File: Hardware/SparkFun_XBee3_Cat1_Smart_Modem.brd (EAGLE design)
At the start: 45.7 x 63.5 mm, 140 parts, among them J1 USB Female Type C Connector, J3 USB Female Type C Connector, J4 QWIIC_RIGHT_ANGLE, Q2 3.1A/30V/105mΩ, U1 FSUSB30MUX_MSOP10, U2 AP63203, U3 ESD Diode, U5 ESD Diode, U6 CP210X

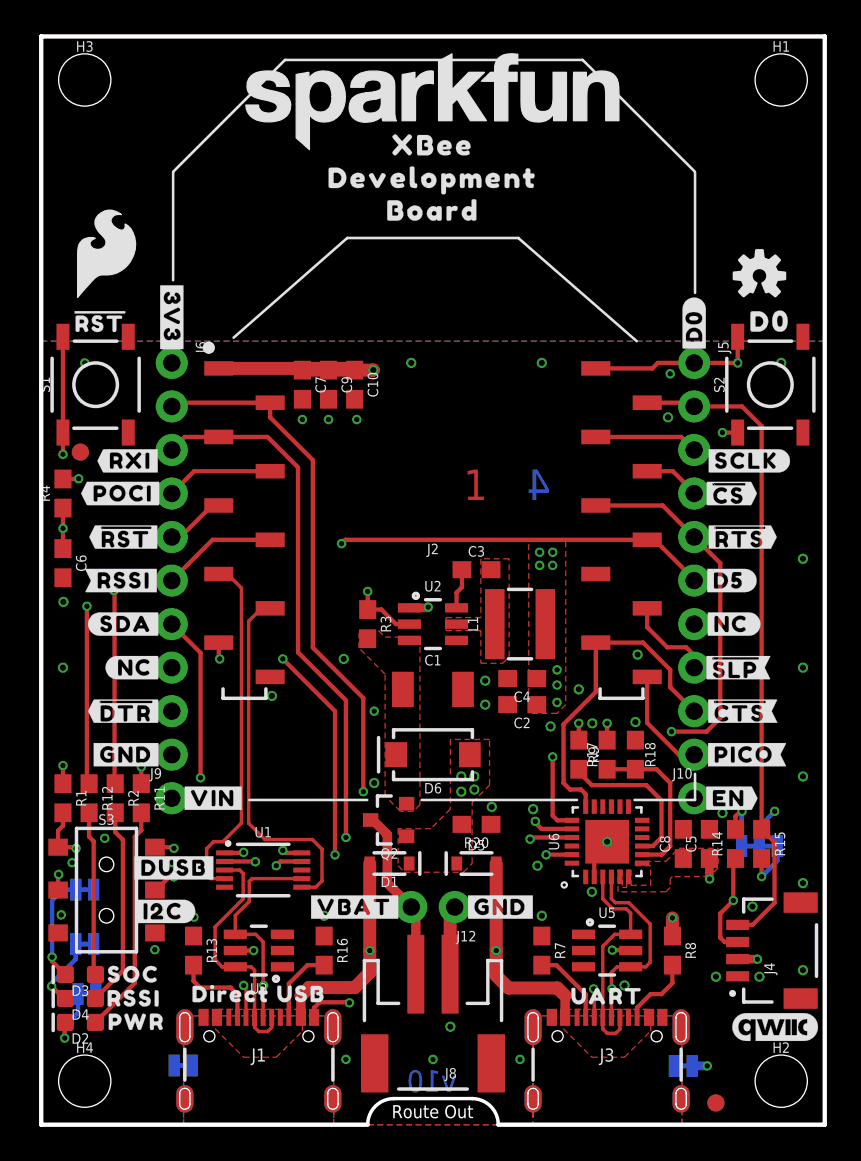
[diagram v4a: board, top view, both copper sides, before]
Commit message: Updates design to use the FT231XS instead of the CP2102N
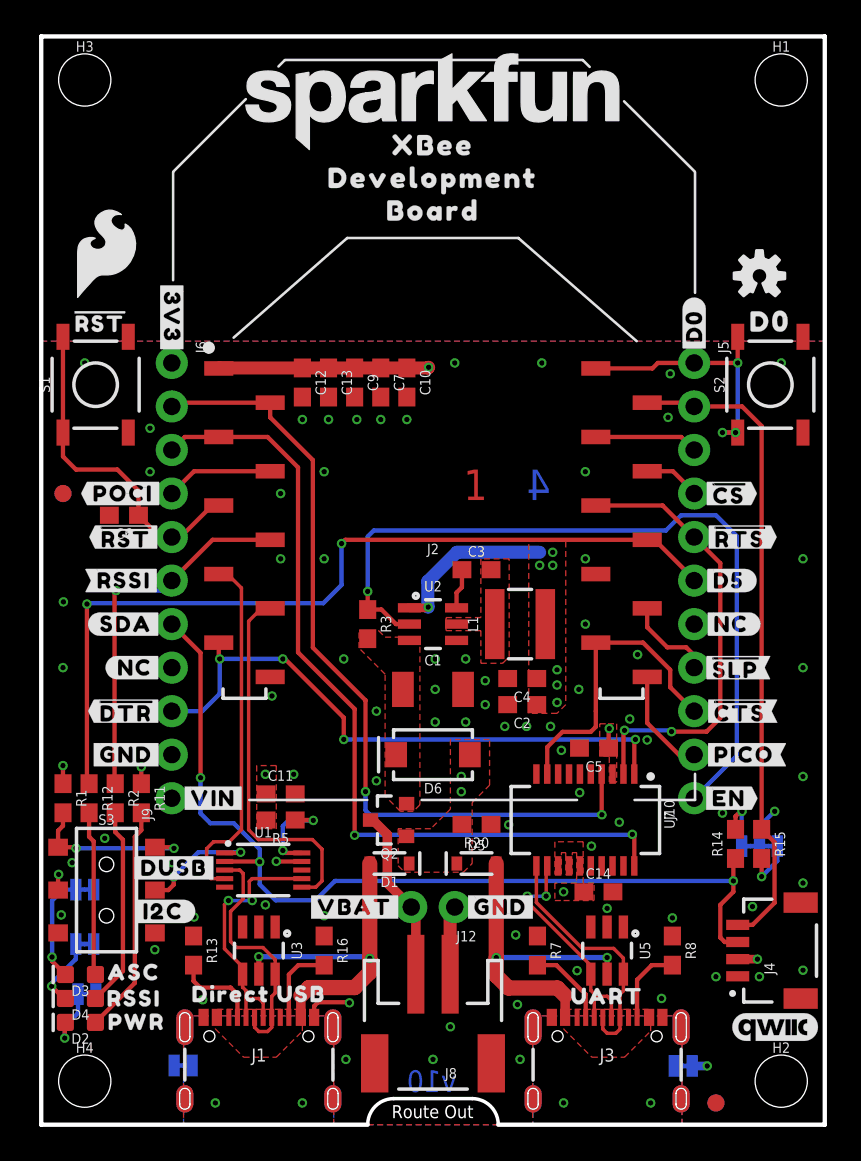
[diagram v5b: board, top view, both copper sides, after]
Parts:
- removed C8: 4.7uF, SparkFun-Capacitors:0603
- removed R17: 22k, SparkFun-Resistors:0603
- removed R18: 33k, SparkFun-Resistors:0603
- removed R4, R9: 10k, SparkFun-Resistors:0603
- removed U$19: (no value), top:#D2#AD2#19
- removed U$33: (no value), top:#SCLK#18
- removed U6: CP210X, SparkFun-IC-Comms:QFN24
- added C11, C14: 0.1uF, SparkFun-Capacitors:0603
- added C12: 10pF, SparkFun-Capacitors:0603
- added C13: 47pF, SparkFun-Capacitors:0603
- added R5: 100, SparkFun-Resistors:0603
- added U7: FT231XS, SparkFun-IC-Comms:SSOP20_L
- D4: value BLUE -> Yellow
- U$1: device top:#RXI#14 -> top:#D2#AD2#SCLK#19
- U$43: device topmirror:SOC30 -> top:ASC32
- moved U$1 26.6 mm to (31.8, 39.4), flipped to the bottom
- moved C5 8.75 mm to (32.3, 22.0), turned to 180 degrees
- moved C7 4.57 mm to (19.8, 43.3)
- moved C6 4.52 mm to (4.83, 35.6), turned to 180 degrees
- moved C10 3.05 mm to (21.3, 43.3)
- moved FD1 2.62 mm to (1.27, 36.8)
- moved FD2 2.62 mm to (1.27, 36.8)
- moved C9 1.53 mm to (18.3, 43.3)
- moved R7 0.25 mm to (29.0, 10.2)
- moved U$43 0.13 mm to (5.41, 8.89)
- turned J10 to 90 degrees
- turned J9 to 90 degrees
- turned U3 to 180 degrees
- turned U5 to 180 degrees
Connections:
- removed net N$10: R17.1, R18.2, U6.8
- removed net N$9: R9.2, U6.9
- new net N$3: R5.1, U1.10
- net !RESET!: no longer R4.1
- net 3.3V: now also C11.1, C12.1, C13.1, C14.1, R5.2; no longer C8.1, R4.2, R9.1, U1.10, U6.5, U6.6, U6.7
- net D+: now also U7.11; no longer U6.3
- net D-: now also U7.12; no longer U6.4
- net D13/TXO: now also U7.4; no longer U6.20
- net D14/RXI: now also U7.20; no longer U6.21
- net D6/!RTS!: now also U7.2; no longer U6.19
- net D7/!CTS!: now also U7.9; no longer U6.18
- net D8/!DTR!: now also U7.1; no longer U6.23
- net GND: now also C11.2, C12.2, C13.2, C14.2, U7.13, U7.14, U7.15, U7.16, U7.3, U7.6; no longer C8.2, R18.1, U6.2, U6.PAD
- net VIN: no longer R17.2
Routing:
- net VIN: track 28.2 -> 17.4 mm, vias 5 -> 2
- net N$10: track 9.54 -> 0.00 mm
- net N$9: track 9.17 -> 0.00 mm
- net D6/!RTS!: track 33.1 -> 26.2 mm
- net N$3: track 0.00 -> 5.57 mm, vias 0 -> 2
- net D14/RXI: track 44.4 -> 49.4 mm
- net D13/TXO: track 44.1 -> 48.2 mm
- net !RESET!: track 23.6 -> 20.1 mm, vias 2 -> 0
- net GND: track 12.7 -> 9.42 mm, vias 53 -> 77
- net 3.3V: track 31.8 -> 29.2 mm, vias 17 -> 15
- net D+: track 13.1 -> 14.7 mm
- net D7/!CTS!: track 19.2 -> 17.8 mm
- net D8/!DTR!: track 36.4 -> 35.2 mm
- net DIRECT_D-: track 15.9 -> 15.1 mm
- net D0: vias 2 -> 3
- added copper zone on layer 15, net SHLD
- added copper zone on layer 2, net SHLD
- added copper zone on layer 15, net SHLD1
- added copper zone on layer 2, net SHLD1

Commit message: Adds new 3.9uH Inductor
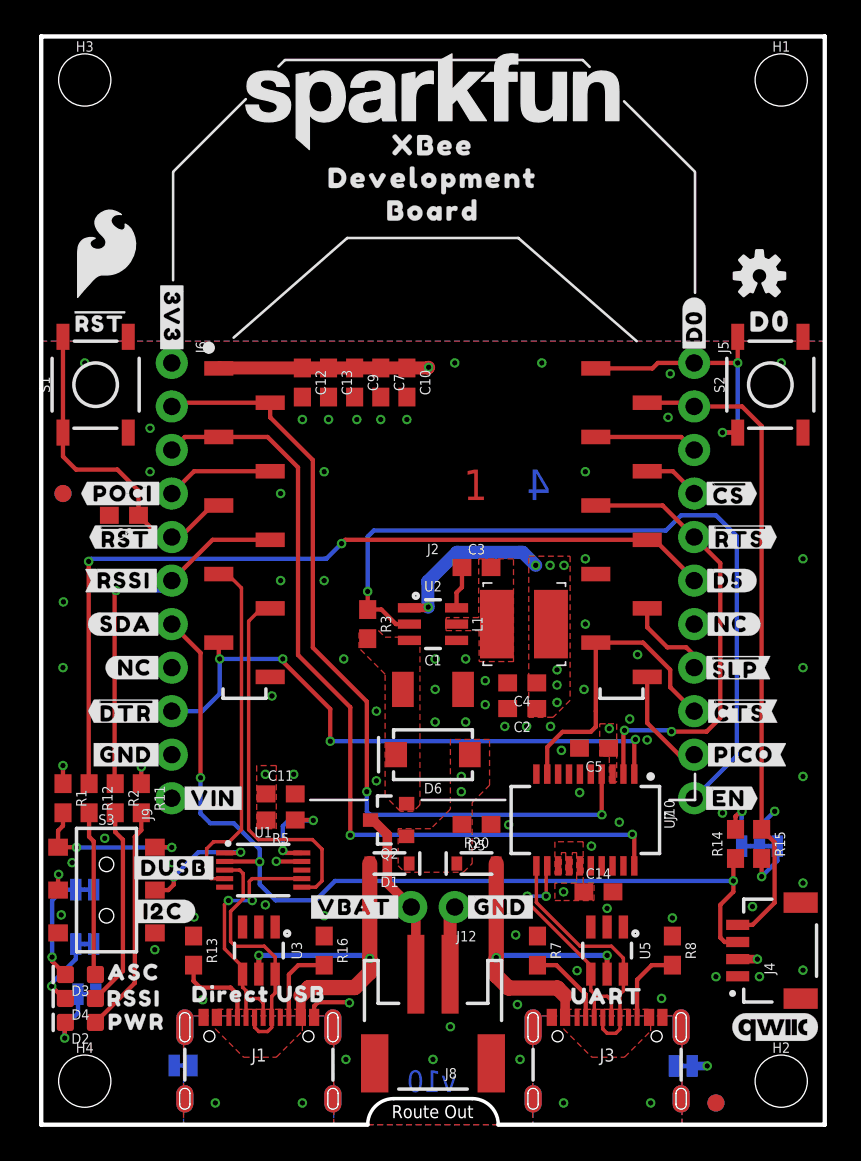
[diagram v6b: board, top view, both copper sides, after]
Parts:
- L1: value 4.7μH -> 3.9uH; device SparkFun-Coils:INDUCTOR_4X4MM -> SparkFun-Coils:INDUCTOR_3.9UH
- moved C4 0.25 mm to (28.1, 25.8)
- moved L1 0.25 mm to (28.2, 29.2)
- moved C2 0.23 mm to (28.1, 24.3)
- moved C3 0.13 mm to (25.4, 32.5)
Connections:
- net 3.3V: now also U7.13, U7.14, U7.15, U7.3
- net GND: no longer U7.13, U7.14, U7.15, U7.3
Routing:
- net 3.3V: track 29.2 -> 27.8 mm
- net D-: track 14.2 -> 13.7 mm
- net D8/!DTR!: track 35.2 -> 35.7 mm
- net D0: vias 3 -> 2

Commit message: Fixes swapped labels on LED jumpers
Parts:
- moved U$27 3.17 mm to (6.10, 13.7)
- moved U$64 3.17 mm to (5.97, 10.5)
- moved U$63 1.27 mm to (22.9, 59.7)
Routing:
- net GND: vias 77 -> 80
- removed copper zone on layer 15, net VIN
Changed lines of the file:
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@@
 <setting verticaltext="up"/>
 </settings>
-<grid distance="0.05" unitdist="inch" unit="inch" style="dots" multiple="1" display="yes" altdistance="0.001" altunitdist="inch" altunit="inch"/>
+<grid distance="0.05" unitdist="inch" unit="inch" style="dots" multiple="1" display="yes" altdistance="0.005" altunitdist="inch" altunit="inch"/>
 <layers>
 <layer number="1" name="Top" color="4" fill="1" visible="yes" active="yes"/>
@@
 <layer number="39" name="tKeepout" color="4" fill="11" visible="no" active="yes"/>
 <layer number="40" name="bKeepout" color="1" fill="11" visible="no" active="yes"/>
-<layer number="41" name="tRestrict" color="4" fill="10" visible="yes" active="yes"/>
+<layer number="41" name="tRestrict" color="4" fill="10" visible="no" active="yes"/>
 <layer number="42" name="bRestrict" color="1" fill="10" visible="no" active="yes"/>
 <layer number="43" name="vRestrict" color="2" fill="10" visible="no" active="yes"/>
@@
 <layer number="115" name="ReferenceISLANDS" color="7" fill="1" visible="no" active="yes"/>
 <layer number="116" name="Patch_BOT" color="9" fill="4" visible="no" active="yes"/>
-<layer number="117" name="PM_Ref" color="26" fill="1" visible="no" active="yes"/>
+<layer number="117" name="PM_Ref" color="26" fill="1" visible="yes" active="yes"/>
 <layer number="118" name="Rect_Pads" color="7" fill="1" visible="no" active="yes"/>
-<layer number="119" name="PF_Ref" color="31" fill="1" visible="no" active="yes"/>
-<layer number="120" name="WFL_Ref" color="25" fill="1" visible="no" active="yes"/>
+<layer number="119" name="PF_Ref" color="31" fill="1" visible="yes" active="yes"/>
+<layer number="120" name="WFL_Ref" color="25" fill="1" visible="yes" active="yes"/>
 <layer number="121" name="_tsilk" color="7" fill="1" visible="no" active="yes"/>
 <layer number="122" name="_bsilk" color="7" fill="1" visible="no" active="yes"/>
@@
 <element name="U$2" library="top" package="##RST##15" value="" x="4.953" y="34.29" smashed="yes"/>
 <element name="U$37" library="top" package="#VBAT#5" value="" x="18.288" y="12.7" smashed="yes" rot="MR0"/>
-<element name="U$27" library="top" package="#ALED#21" value="" x="6.096" y="10.541" smashed="yes" rot="MR0"/>
+<element name="U$27" library="top" package="#ALED#21" value="" x="6.096" y="13.716" smashed="yes" rot="MR0"/>
 <element name="U$54" library="top" package="#PLED#20" value="" x="5.969" y="7.62" smashed="yes" rot="MR0"/>
 <element name="U$55" library="top" package="#D0#AD0#18" value="" x="33.909" y="44.45" smashed="yes" rot="MR0"/>
@@
 <element name="U$65" library="top" package="UART32" value="" x="33.02" y="7.493" smashed="yes"/>
 <element name="U$30" library="top" package="#RST#30" value="" x="3.429" y="46.863" smashed="yes"/>
-<element name="U$63" library="SparkFun-Aesthetics" package="SFE_LOGO_NAME_.2" value="" x="21.59" y="59.69" smashed="yes" rot="MR0"/>
+<element name="U$63" library="SparkFun-Aesthetics" package="SFE_LOGO_NAME_.2" value="" x="22.86" y="59.69" smashed="yes" rot="MR0"/>
 <element name="U$61" library="SparkFun-Aesthetics" package="SFE_LOGO_FLAME_.2" value="" x="3.81" y="50.8" smashed="yes"/>
 <element name="D4" library="SparkFun-LED" package="LED-0603" value="Yellow" x="2.286" y="7.366" smashed="yes" rot="R180">
@@
 </element>
 <element name="U$62" library="top" package="RSSI31" value="" x="5.4102" y="7.366" smashed="yes"/>
-<element name="U$64" library="top" package="#RLED#22" value="" x="5.969" y="13.716" smashed="yes" rot="MR0"/>
+<element name="U$64" library="top" package="#RLED#22" value="" x="5.969" y="10.541" smashed="yes" rot="MR0"/>
 <element name="U$14" library="top" package="#POCI#D12#24" value="" x="12.319" y="36.83" smashed="yes" rot="MR0"/>
 <element name="U$29" library="top" package="#POCI#23" value="" x="4.7752" y="36.83" smashed="yes"/>
@@
 <via x="27.7876" y="7.0104" extent="1-16" drill="0.3048"/>
 <via x="9.4234" y="7.2898" extent="1-16" drill="0.3048"/>
+<via x="36.8554" y="14.986" extent="1-16" drill="0.3048"/>
+<via x="17.1196" y="15.0368" extent="1-16" drill="0.3048"/>
+<via x="27.9146" y="15.0622" extent="1-16" drill="0.3048"/>
 </signal>
 <signal name="3.3V">
@@
 <wire x1="8.0264" y1="18.6436" x2="23.7236" y2="18.6436" width="0.762" layer="15"/>
 <wire x1="23.7236" y1="18.6436" x2="24.511" y2="19.431" width="0.762" layer="15"/>
-<polygon width="0.127" layer="15" spacing="0.127" thermals="no">
-<vertex x="23.876" y="22.479"/>
-<vertex x="23.876" y="18.542"/>
-<vertex x="24.892" y="18.542"/>
-<vertex x="26.162" y="19.812"/>
-<vertex x="26.162" y="22.479"/>
-</polygon>
 </signal>
 <signal name="ALED">

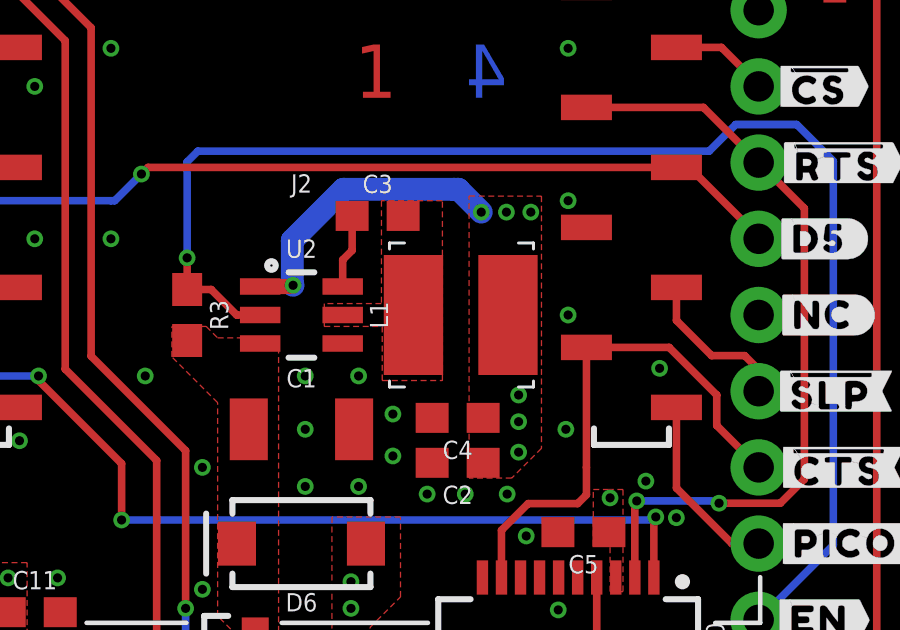
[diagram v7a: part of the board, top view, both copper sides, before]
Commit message: Fixes silk width on inductor, shifts part to correct keepout errors
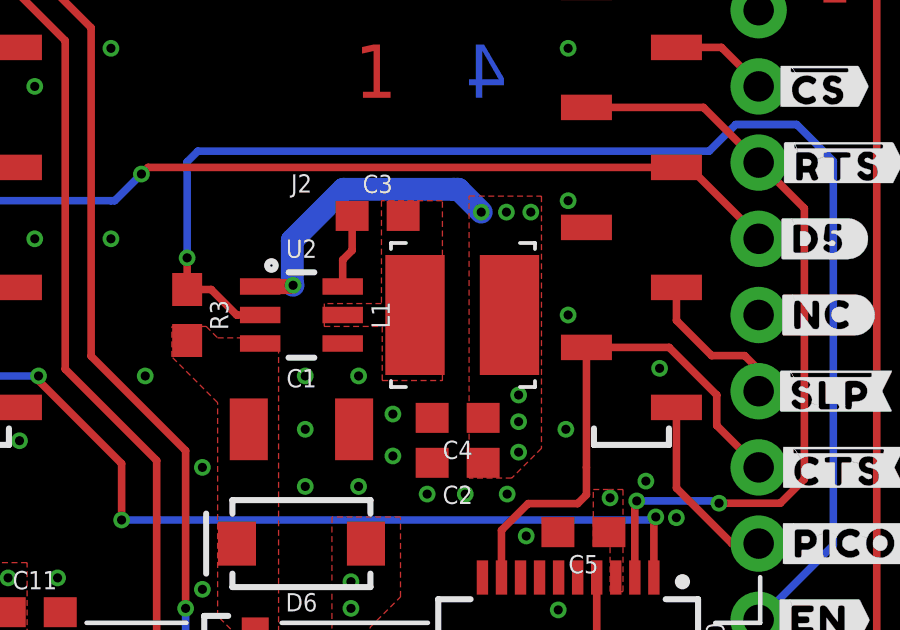
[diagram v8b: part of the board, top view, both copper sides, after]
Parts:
- moved L1 0.05 mm to (28.2, 29.2)
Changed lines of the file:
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@@
 <setting verticaltext="up"/>
 </settings>
-<grid distance="0.05" unitdist="inch" unit="inch" style="dots" multiple="1" display="yes" altdistance="0.005" altunitdist="inch" altunit="inch"/>
+<grid distance="0.05" unitdist="inch" unit="inch" style="dots" multiple="1" display="yes" altdistance="0.001" altunitdist="inch" altunit="inch"/>
 <layers>
 <layer number="1" name="Top" color="4" fill="1" visible="yes" active="yes"/>
@@
 <layer number="37" name="tTest" color="7" fill="1" visible="no" active="yes"/>
 <layer number="38" name="bTest" color="7" fill="1" visible="no" active="yes"/>
-<layer number="39" name="tKeepout" color="4" fill="11" visible="no" active="yes"/>
+<layer number="39" name="tKeepout" color="4" fill="11" visible="yes" active="yes"/>
 <layer number="40" name="bKeepout" color="1" fill="11" visible="no" active="yes"/>
 <layer number="41" name="tRestrict" color="4" fill="10" visible="no" active="yes"/>
@@
 <attribute name="VALUE" x="22.86" y="26.67" size="0.6096" layer="27" font="vector" ratio="20" align="bottom-center"/>
 </element>
-<element name="L1" library="SparkFun-Coils" package="INDUCTOR_3.9UH" value="3.9uH" x="28.194" y="29.21" smashed="yes" rot="R90">
-<attribute name="NAME" x="25.752" y="29.21" size="0.6096" layer="25" font="vector" ratio="20" rot="R90" align="bottom-center"/>
-<attribute name="PROD_ID" value="NDUC-18014" x="25.654" y="22.86" size="1.778" layer="27" rot="R90" display="off"/>
-<attribute name="VALUE" value="3.9uH" x="30.607" y="29.21" size="0.6096" layer="27" font="vector" ratio="20" rot="R90" align="top-center"/>
+<element name="L1" library="SparkFun-Coils" package="INDUCTOR_3.9UH" value="3.9uH" x="28.2448" y="29.21" smashed="yes" rot="R90">
+<attribute name="NAME" x="25.8028" y="29.21" size="0.6096" layer="25" font="vector" ratio="20" rot="R90" align="bottom-center"/>
+<attribute name="PROD_ID" value="NDUC-18014" x="25.7048" y="22.86" size="1.778" layer="27" rot="R90" display="off"/>
+<attribute name="VALUE" value="3.9uH" x="30.6578" y="29.21" size="0.6096" layer="27" font="vector" ratio="20" rot="R90" align="top-center"/>
 </element>
 <element name="C3" library="SparkFun-Capacitors" package="0603" value="0.1uF" x="25.4" y="32.512" smashed="yes">
@@
 <wire x1="27.94" y1="33.401" x2="28.0924" y2="33.401" width="0.762" layer="16"/>
 <wire x1="28.0924" y1="33.401" x2="28.8544" y2="32.639" width="0.762" layer="16"/>
+<wire x1="30.099" y1="26.543" x2="29.7948" y2="29.21" width="0" layer="19" extent="1-1"/>
+<wire x1="33.108" y1="21.971" x2="33.147" y2="23.114" width="0" layer="19" extent="1-1"/>
+<wire x1="13.12" y1="19.304" x2="13.081" y2="20.447" width="0" layer="19" extent="1-1"/>
+<wire x1="28.917" y1="25.781" x2="30.099" y2="25.654" width="0" layer="19" extent="1-1"/>
+<wire x1="31.662" y1="13.589" x2="30.48" y2="13.589" width="0" layer="19" extent="1-1"/>
+<wire x1="28.917" y1="24.2824" x2="30.099" y2="24.638" width="0" layer="19" extent="1-1"/>
+<wire x1="33.3375" y1="20.4597" x2="33.108" y2="21.971" width="0" layer="19" extent="1-1"/>
+<wire x1="31.4325" y1="15.1003" x2="31.662" y2="13.589" width="0" layer="19" extent="1-1"/>
+<wire x1="30.7975" y1="15.1003" x2="31.4325" y2="15.1003" width="0" layer="19" extent="1-1"/>
+<wire x1="30.1625" y1="15.1003" x2="30.7975" y2="15.1003" width="0" layer="19" extent="1-1"/>
+<wire x1="13.12" y1="17.78" x2="13.12" y2="19.304" width="0" layer="19" extent="1-1"/>
 </signal>
 <signal name="V_USB">
@@
 <vertex x="23.622" y="29.591"/>
 </polygon>
+<wire x1="26.6448" y1="29.21" x2="26.25" y2="32.512" width="0" layer="19" extent="1-1"/>
+<wire x1="24.2351" y1="29.21" x2="26.6448" y2="29.21" width="0" layer="19" extent="1-1"/>
 </signal>
 <signal name="EN">
